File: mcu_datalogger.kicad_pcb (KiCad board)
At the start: 2 copper layers, 50.6 x 30.6 mm, 29 parts, among them J1 Conn_01x04_Pin, J2 Conn_01x04_Pin, J3 Conn_01x09, J4 Conn_02x03_Counter_Clockwise, U1 DS1337S_, U3 24LC1025, U4 24LC1025, U5 ATMEGA328P-AU, Y1 32.768 KHz, Y2 16MHz

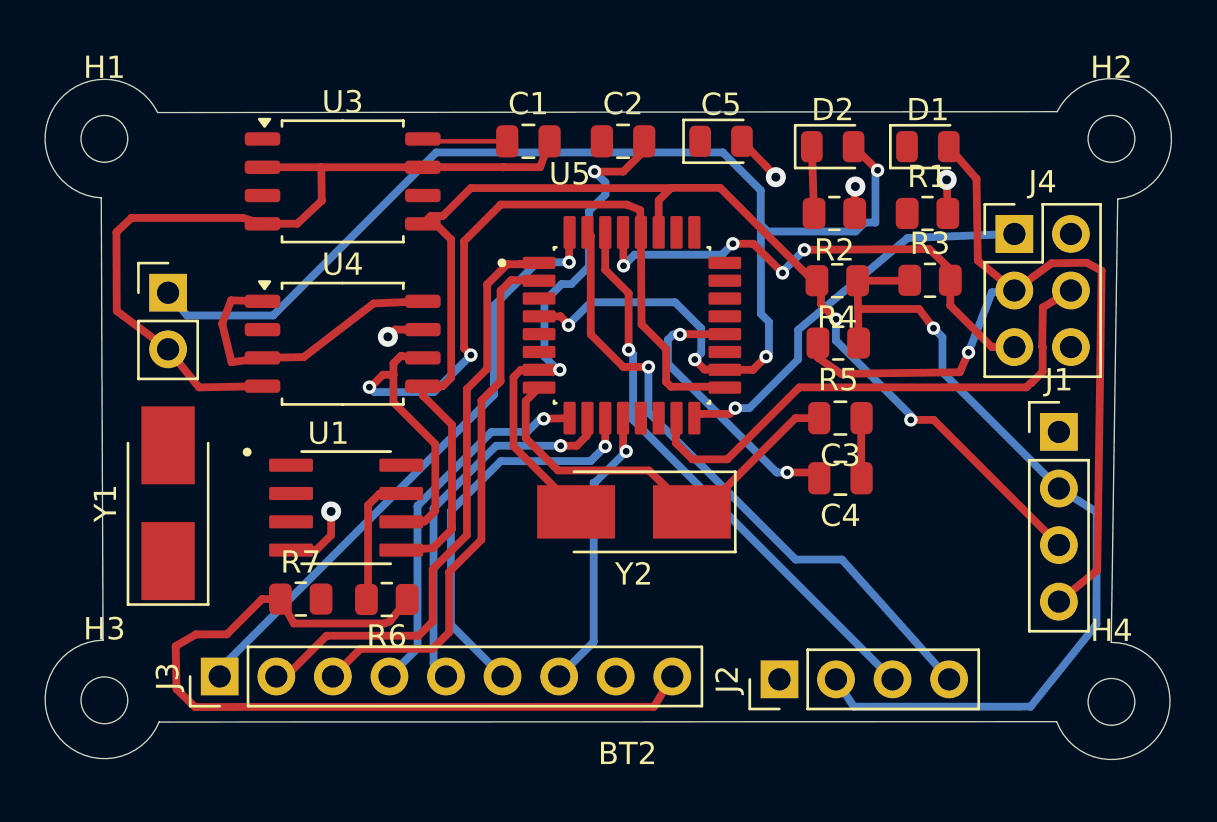
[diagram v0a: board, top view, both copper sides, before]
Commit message: Add board hardware image and update README
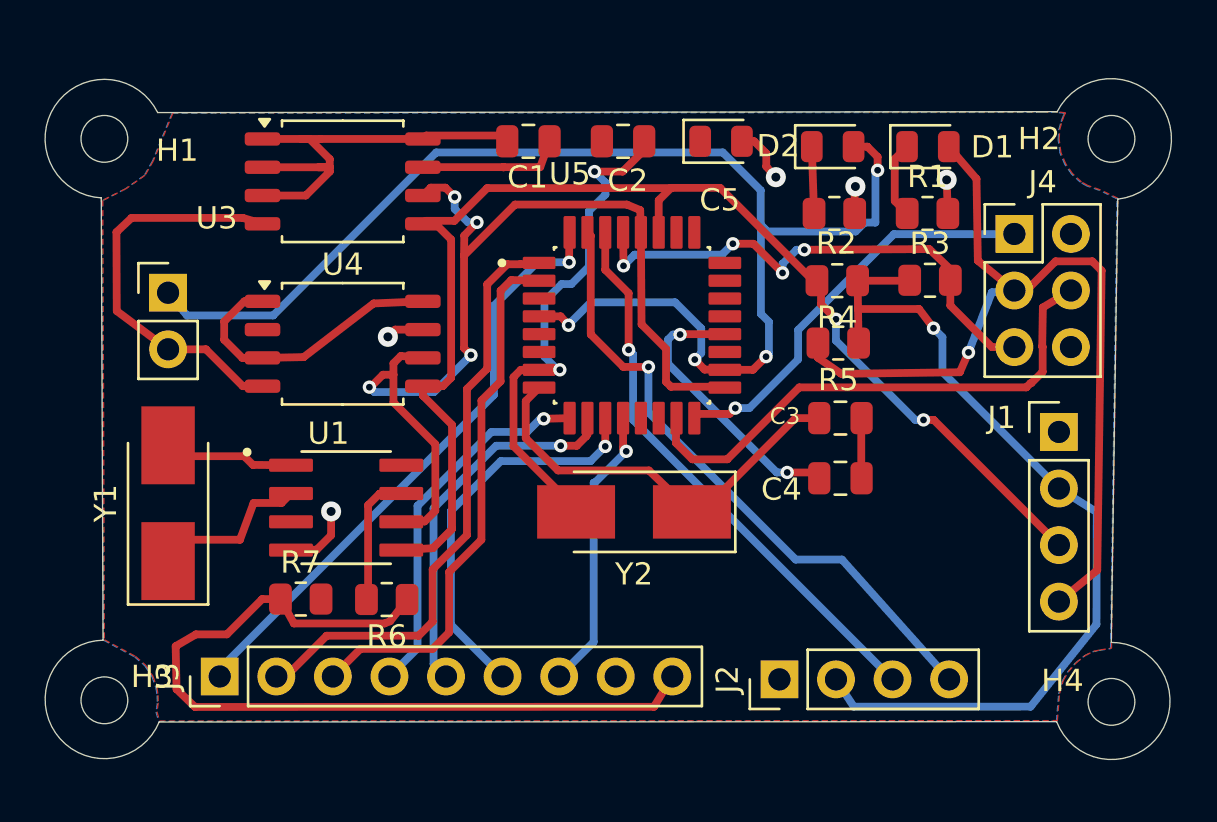
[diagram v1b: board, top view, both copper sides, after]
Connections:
- net Net-(D1-K) renamed /R1_1
- net Net-(U1-X1) renamed /X1
- net Net-(U1-X2) renamed /X2
- BT2 pad 1: Net-(BT2-+) -> /AVCC
- C5 pad 1: Net-(BT2-+) -> /AVCC
- D1 pad 2: Net-(BT2-+) -> /AVCC
- D2 pad 2: Net-(BT2-+) -> /SCK
- J4 pad 2: /Vcc -> /SCK
- J4 pad 3: /SCK -> /RESET
- J4 pad 4: /MOSI -> GND
- J4 pad 5: /RESET -> /MOSI
- U5 pad 18: Net-(BT2-+) -> /AVCC
- U5 pad 4: Net-(BT2-+) -> /AVCC
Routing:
- net /SCK: track 82.6 -> 150.2 mm, vias 3 -> 9
- net Net-(BT2-+): track 62.1 -> 0.00 mm, vias 4 -> 0
- net /Vcc: track 95.0 -> 110.8 mm
- net GND: track 49.2 -> 37.7 mm
- net /X2: track 0.00 -> 7.24 mm
- net /X1: track 0.00 -> 5.88 mm
- net /R1_1: track 0.00 -> 3.46 mm
- added copper zone on F.Cu, net /Vcc
- added copper zone on B.Cu, net GND
